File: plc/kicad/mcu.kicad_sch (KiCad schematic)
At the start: 6 parts, among them U2 ESP32-S3-MINI-1U

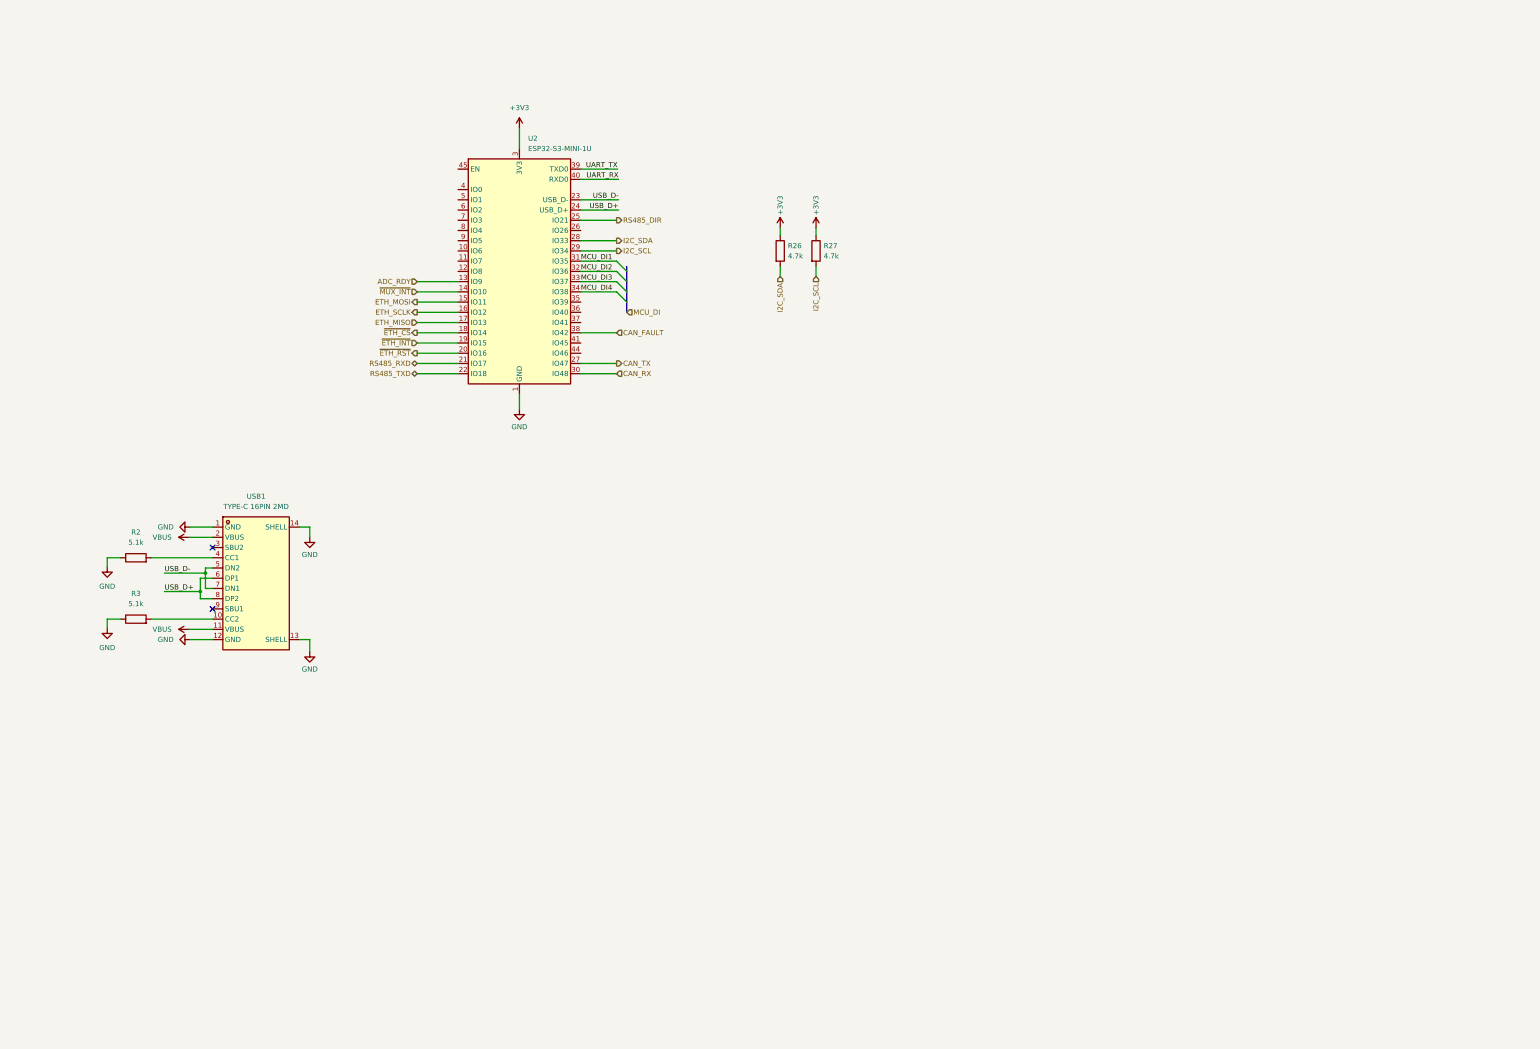
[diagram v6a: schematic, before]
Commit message: Added CP2102N bridge
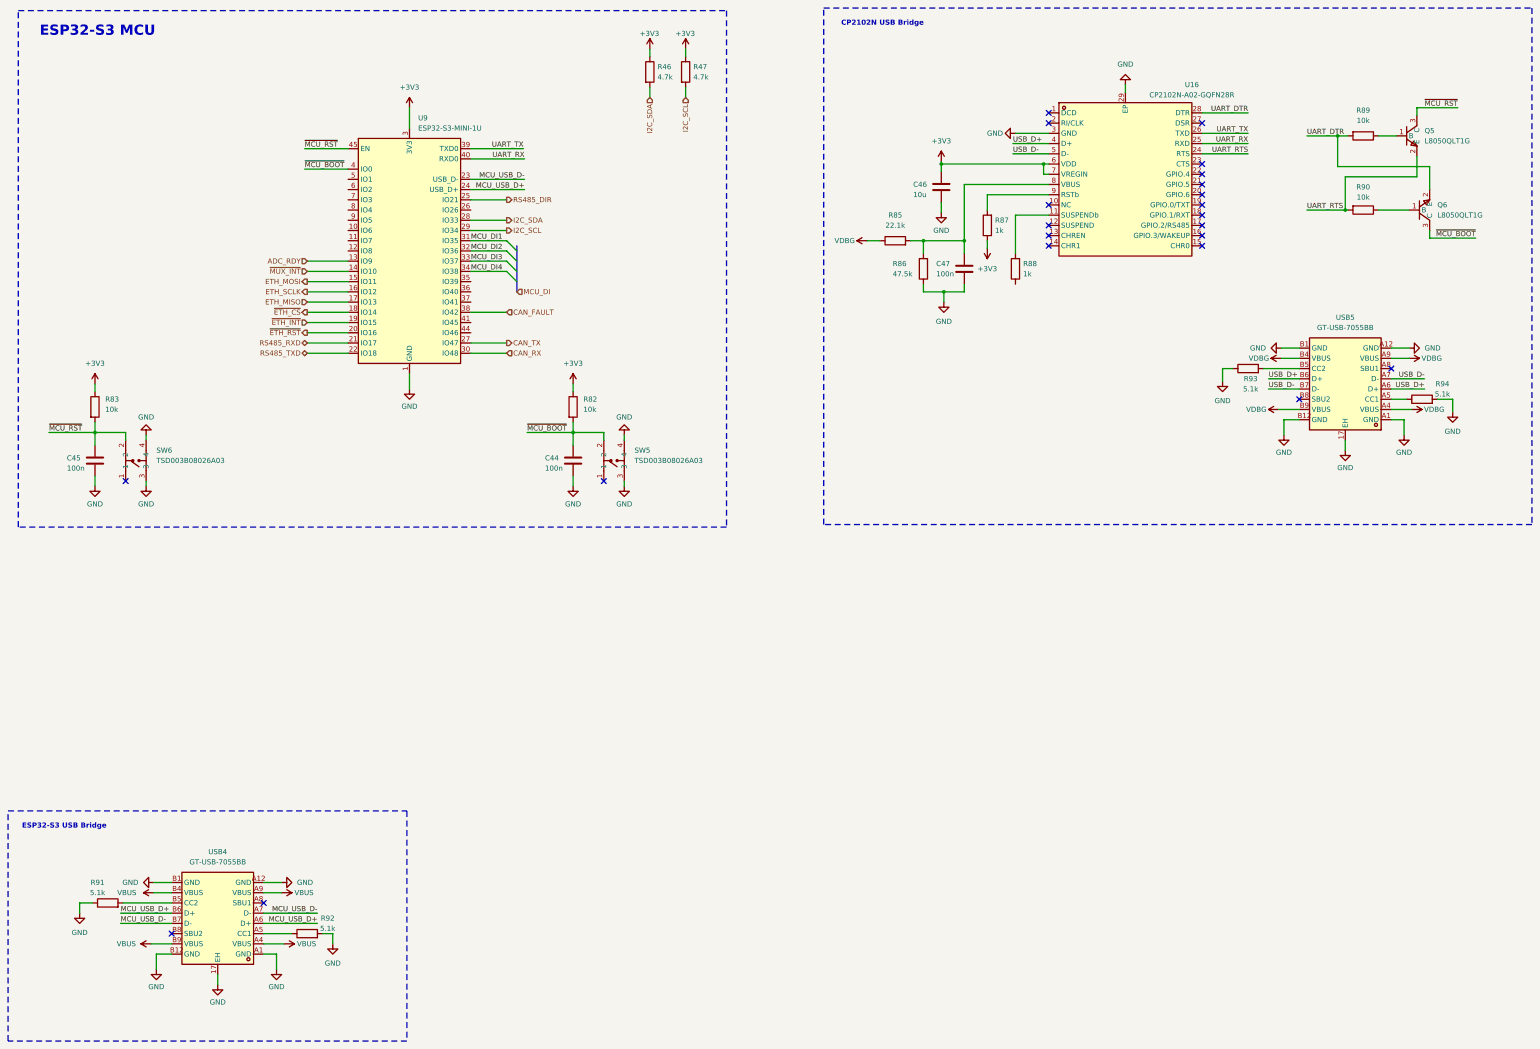
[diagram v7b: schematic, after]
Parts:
- removed R2, R3: 5.1k, Resistor_SMD:R_0805_2012Metric_Pad1.20x1.40mm_HandSolder, symbol Device:R
- removed USB1: TYPE-C 16PIN 2MD, LibrePLC32:USB-C-SMD_TYPE-C-6PIN-2MD-073, symbol LibrePLC32:TYPE-C16PIN2MD
- added C44, C45, C47: 100n, Capacitor_SMD:C_0805_2012Metric, symbol Device:C
- added C46: 10u, Capacitor_SMD:C_0805_2012Metric, symbol Device:C
- added Q5, Q6: L8050QLT1G, LibrePLC32:SOT-23-3_L2.9-W1.3-P1.90-LS2.4-BR, symbol LibrePLC32:L8050QLT1G
- added R82, R83: 10k, Resistor_SMD:R_0805_2012Metric, symbol Device:R
- added R85: 22.1k, Resistor_SMD:R_0805_2012Metric_Pad1.20x1.40mm_HandSolder, symbol Device:R
- added R86: 47.5k, Resistor_SMD:R_0805_2012Metric_Pad1.20x1.40mm_HandSolder, symbol Device:R
- added R87, R88: 1k, Resistor_SMD:R_0805_2012Metric_Pad1.20x1.40mm_HandSolder, symbol Device:R
- added R89, R90: 10k, Resistor_SMD:R_0805_2012Metric_Pad1.20x1.40mm_HandSolder, symbol Device:R
- added R91, R92, R93, R94: 5.1k, Resistor_SMD:R_0805_2012Metric_Pad1.20x1.40mm_HandSolder, symbol Device:R
- added SW5, SW6: TSD003B08026A03, LibrePLC32:SW-SMD_4P-L6.0-W6.0-P4.50-LS8.6, symbol LibrePLC32:TSD003B08026A03
- added U16: CP2102N-A02-GQFN28R, LibrePLC32:QFN-28_L5.0-W5.0-P0.50-TL-EP3.3, symbol LibrePLC32:CP2102N-A02-GQFN28R
- added USB4, USB5: GT-USB-7055BB, LibrePLC32:USB-C-TH_GT-USB-7055BB, symbol LibrePLC32:GT-USB-7055BB
- renumbered R26 to R46, R27 to R47, U2 to U9
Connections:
- net +3V3: now also C46.2, R82.1, R83.1, R87.1, U16.6 (VDD), U16.7 (VREGIN)
- net GND: now also C44.1, C45.1, C46.1, C47.2, R86.1, R91.1, R92.2, R93.1, R94.2, SW5.3, SW5.4, SW6.3, SW6.4, U16.29 (EP), U16.3 (GND), USB4.17 (EH), USB4.A1 (GND), USB4.A12 (GND), USB4.B1 (GND), USB4.B12 (GND), USB5.17 (EH), USB5.A1 (GND), USB5.A12 (GND), USB5.B1 (GND), USB5.B12 (GND)
- net UART_RX: now also U16.25 (RXD)
- net UART_TX: now also U16.26 (TXD)
- net USB_D+: now also U16.4 (D+), USB5.A6 (D+), USB5.B6 (D+); no longer U9.24 (USB_D+)
- net USB_D-: now also U16.5 (D-), USB5.A7 (D-), USB5.B7 (D-); no longer U9.23 (USB_D-)
- net VBUS: now also USB4.A4 (VBUS), USB4.A9 (VBUS), USB4.B4 (VBUS), USB4.B9 (VBUS)
- net ~{MCU_BOOT}: now reaches U9.4 (IO0)
- net ~{MCU_BOOT}: now also C44.2, Q6.3 (C), R82.2, SW5.2
- net ~{MCU_RST}: now reaches U9.45 (EN)
- net ~{MCU_RST}: now also C45.2, Q5.3 (C), R83.2, SW6.2
- new net: C47.1, R85.2, R86.2, U16.8 (VBUS)
- new net: R93.2, USB5.B5 (CC2)
- new net: R87.2, U16.9 (RSTb)
- new net: Q6.1 (B), R90.1
- new net: R88.2, U16.11 (SUSPENDb)
- new net: R91.2, USB4.B5 (CC2)
- new net: R92.1, USB4.A5 (CC1)
- new net: R94.1, USB5.A5 (CC1)
- new net: Q5.1 (B), R89.1
- new net MCU_USB_D+: U9.24 (USB_D+), USB4.A6 (D+), USB4.B6 (D+)
- new net MCU_USB_D-: U9.23 (USB_D-), USB4.A7 (D-), USB4.B7 (D-)
- new net UART_DTR: Q6.2 (E), R89.2, U16.28 (DTR)
- new net UART_RTS: Q5.2 (E), R90.2, U16.24 (RTS)
- new net VDBG: R85.1, USB5.A4 (VBUS), USB5.A9 (VBUS), USB5.B4 (VBUS), USB5.B9 (VBUS)
- no-connect marks 2 -> 22
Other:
- note added: "CP2102N USB Bridge"
- note added: "ESP32-S3 MCU"
- note added: "ESP32-S3 USB Bridge"
- moved on the sheet: R46, R47, U9

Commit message: Added 3.3V regulator
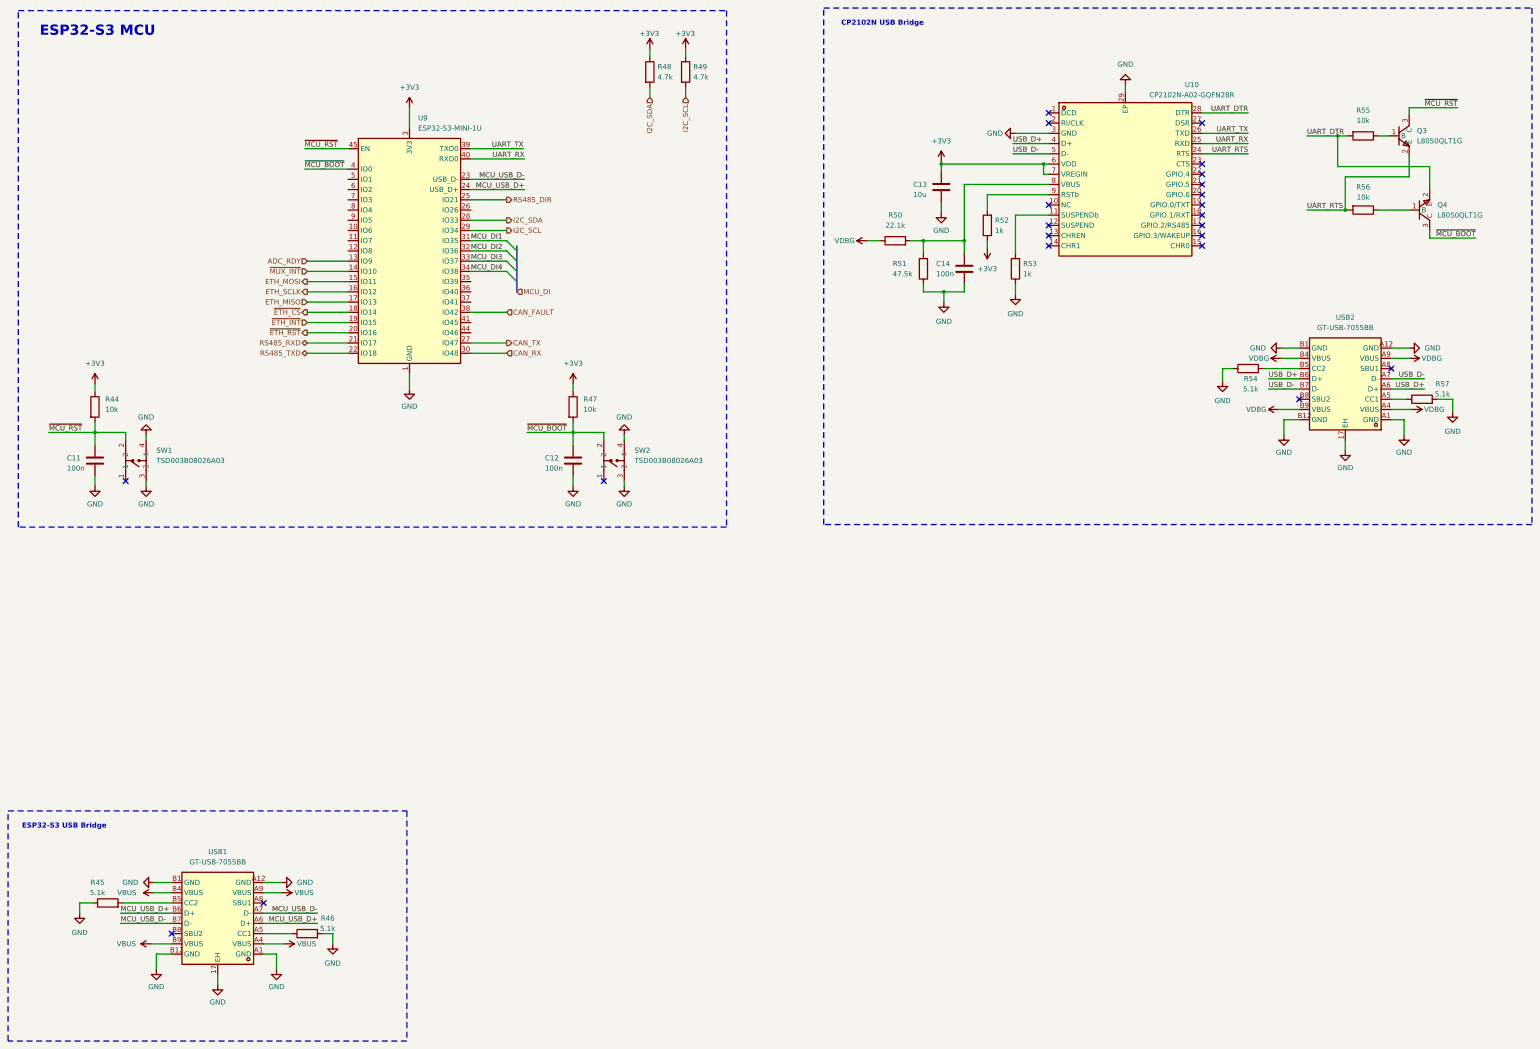
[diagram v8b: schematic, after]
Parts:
- renumbered C45 to C11, C44 to C12, C46 to C13, C47 to C14, Q5 to Q3, Q6 to Q4, R83 to R44, R91 to R45, R92 to R46, R82 to R47, R46 to R48, R47 to R49, R85 to R50, R86 to R51, R87 to R52, R88 to R53, R93 to R54, R89 to R55, R90 to R56, R94 to R57, SW6 to SW1, SW5 to SW2, U16 to U10, USB4 to USB1, USB5 to USB2
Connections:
- net GND: now also R53.1
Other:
- moved on the sheet: Q3
